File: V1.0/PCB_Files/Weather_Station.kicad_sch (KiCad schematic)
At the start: 13 parts, among them U1 STM32F103C8T6

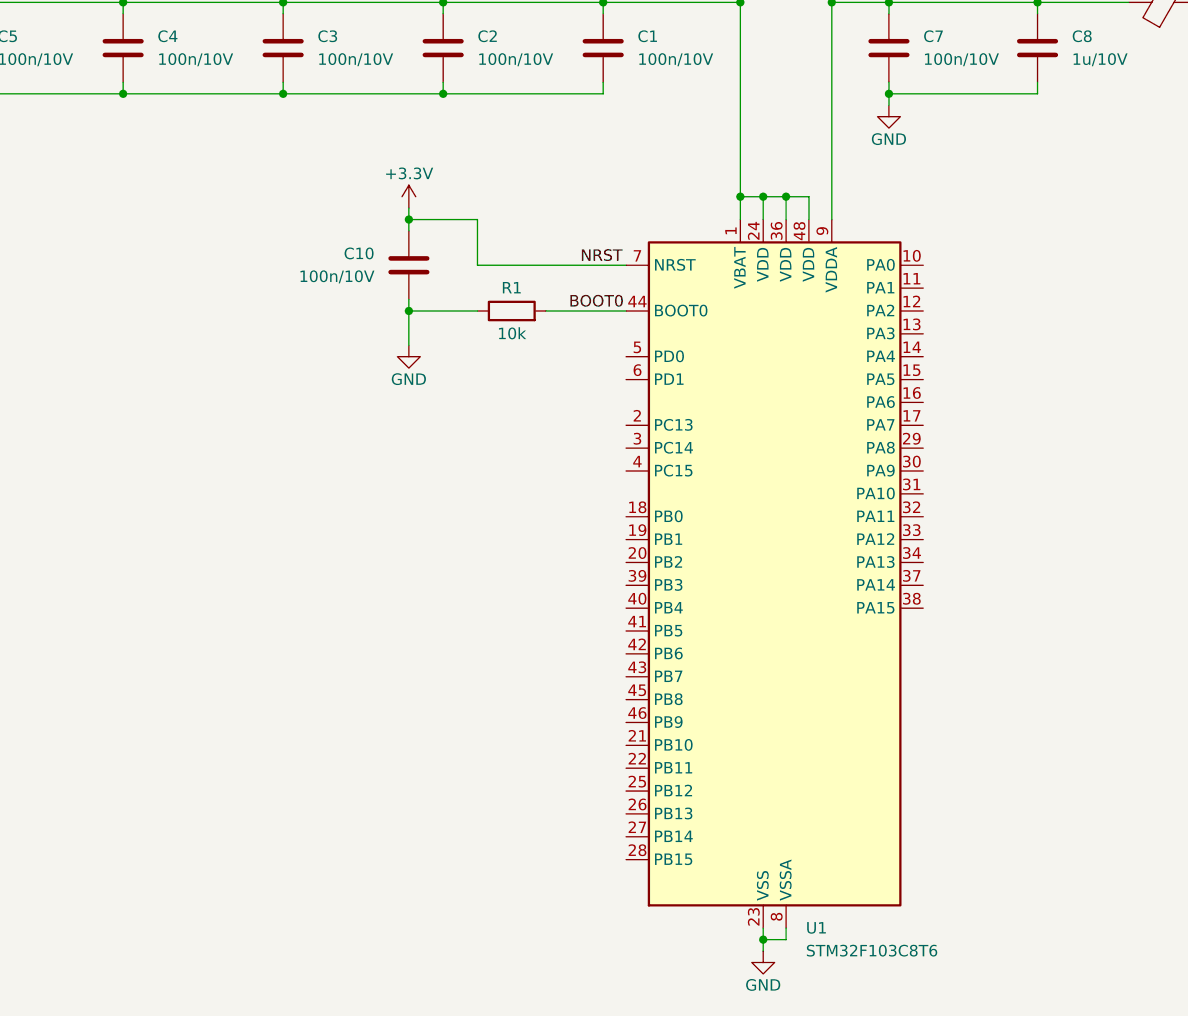
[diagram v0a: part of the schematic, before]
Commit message: Added STM32 Fiormware Directory + Prj. . Added OSC.
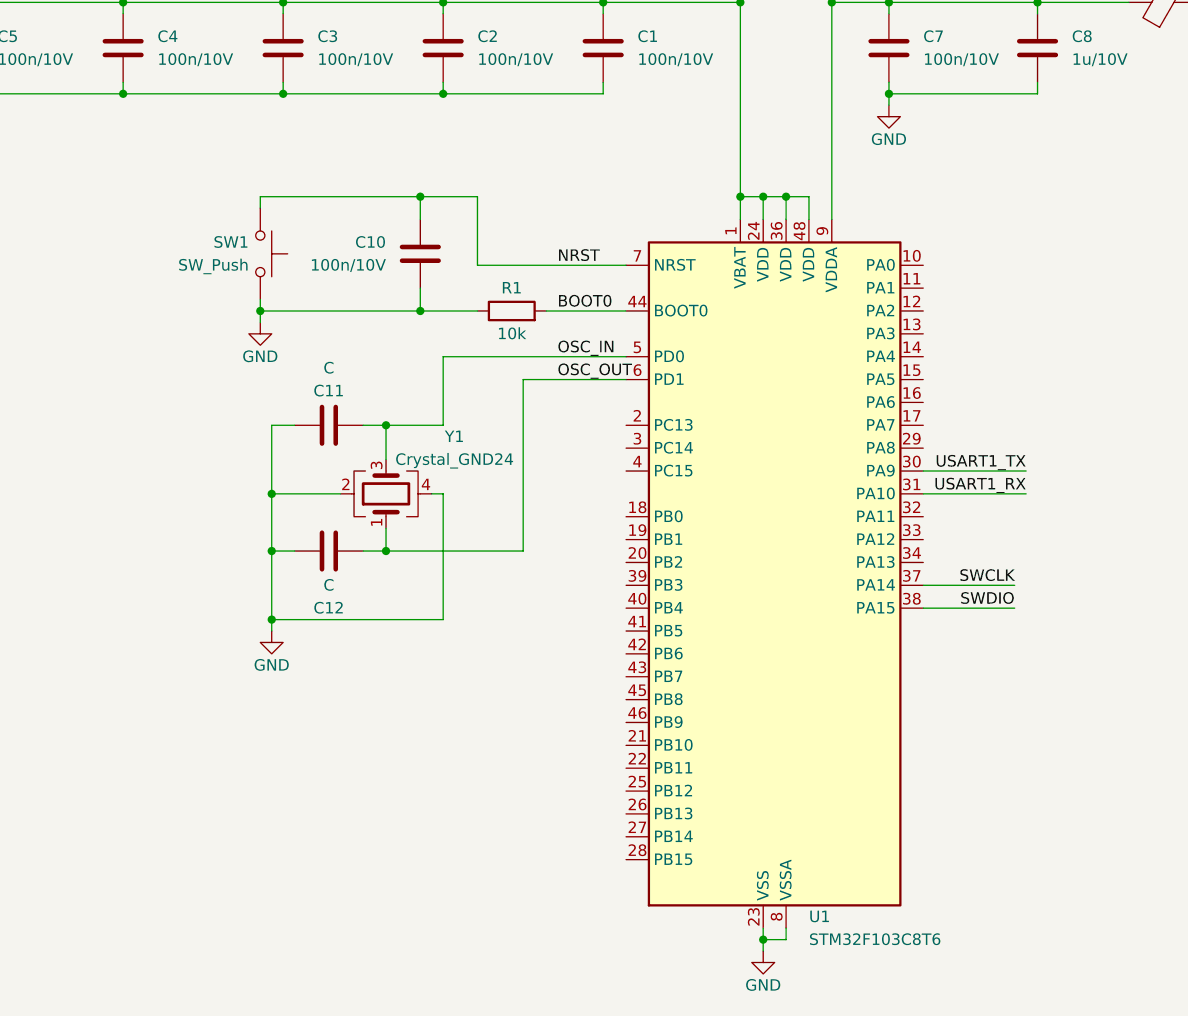
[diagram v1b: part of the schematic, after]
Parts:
- added C11, C12: C, symbol Device:C
- added SW1: SW_Push, symbol Switch:SW_Push
- added Y1: Crystal_GND24, symbol Device:Crystal_GND24
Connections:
- net +3.3V: no longer C10.2, U1.7 (NRST)
- net GND: now also C11.1, C12.2, SW1.2, Y1.2, Y1.4
- net USART1_TX: now reaches U1.30 (PA9)
- net USART1_RX: now reaches U1.31 (PA10)
- net SWCLK: now reaches U1.37 (PA14)
- net SWDIO: now reaches U1.38 (PA15)
- net OSC_IN: now reaches U1.5 (PD0)
- net OSC_IN: now also C11.2, Y1.3
- net OSC_OUT: now reaches U1.6 (PD1)
- net OSC_OUT: now also C12.1, Y1.1
- new net NRST: C10.2, SW1.1, U1.7 (NRST)
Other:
- moved on the sheet: C10

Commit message: Some changes in the IOC and continues Schematic.
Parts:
- added R2, R3: R, symbol Device:R
- added U2: HDC1080DMBR, Package_SON:Texas_PWSON-N6, symbol Sensor_Humidity:HDC1080
- added U3: NHD-C12832A1Z-FSRGB, Display:HY1602E, symbol Display_Graphic:NHD-C12832A1Z-FSRGB
- C11, C12: value C -> 10p/10V
- Y1: value Crystal_GND24 -> X322516MLB4SI
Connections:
- net +3.3V: now also R2.1, R3.1, U2.5 (VCC)
- net GND: now also C12.1, U2.2 (GND); no longer C12.2
- net OSC_OUT: now also C12.2; no longer C12.1
- net I2C1_SCL: now reaches U1.42 (PB6)
- net I2C1_SCL: now also R3.2, U2.6 (SCL)
- net I2C1_SDA: now reaches U1.43 (PB7)
- net I2C1_SDA: now also R2.2, U2.1 (SDA)
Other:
- note added: "Display"
- note added: "Display Stecker auch extern einfügen, falls display nicht geht, dass getestet werden kann."
- note added: "STM32"
- note added: "Sensor"
- note added: "ToDo: Calculate Resistor Values."
- moved on the sheet: C1, C10, C11, C2, C3, C4, C5, C6, C7, C8, C9, FB1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

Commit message: Display Wiring should be finsihed.
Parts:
- removed U3: NHD-C12832A1Z-FSRGB, Display:HY1602E, symbol Display_Graphic:NHD-C12832A1Z-FSRGB
- added C13, C14: 4u7/16V, symbol Device:C
- added C15: 2u2/16V, symbol Device:C
- added C16, C17: 1u/16V, symbol Device:C
- added C18: 100n/10V, symbol Device:C
- added C19, C20: 4u7/10V, symbol Device:C
- added J1: N091-2832TSWFG02-H14, symbol Connector:Conn_01x14_Socket
- added R4: 910k, symbol Device:R
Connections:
- net +3.3V: now also C13.1, C14.1, C18.1, C19.1, C20.1, J1.14 (Pin_14), J1.5 (Pin_5), J1.8 (Pin_8), J1.9 (Pin_9)
- net GND: now also C13.2, C14.2, C15.2, C18.2, C19.2, C20.2, J1.7 (Pin_7), R4.2
- new net C1N: C17.2, J1.4 (Pin_4)
- new net C1P: C17.1, J1.3 (Pin_3)
- new net C2N: C16.2, J1.2 (Pin_2)
- new net C2P: C16.1, J1.1 (Pin_1)
- new net IREF: J1.12 (Pin_12), R4.1
- new net SCL: J1.10 (Pin_10)
- new net SDA: J1.11 (Pin_11)
- new net VCOMH: C15.1, J1.13 (Pin_13)
- no-connect marks 0 -> 1
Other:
- note added: "Display Stiftleisten auch extern einfügen, falls display nicht geht, dass getestet werden kann."
- note added: "R4 nochmal checken."
- note removed: "Display Stecker auch extern einfügen, falls display nicht geht, dass getestet werden kann."

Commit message: Now Display should be finished.
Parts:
- C14: value 4u7/16V -> 100n/16V

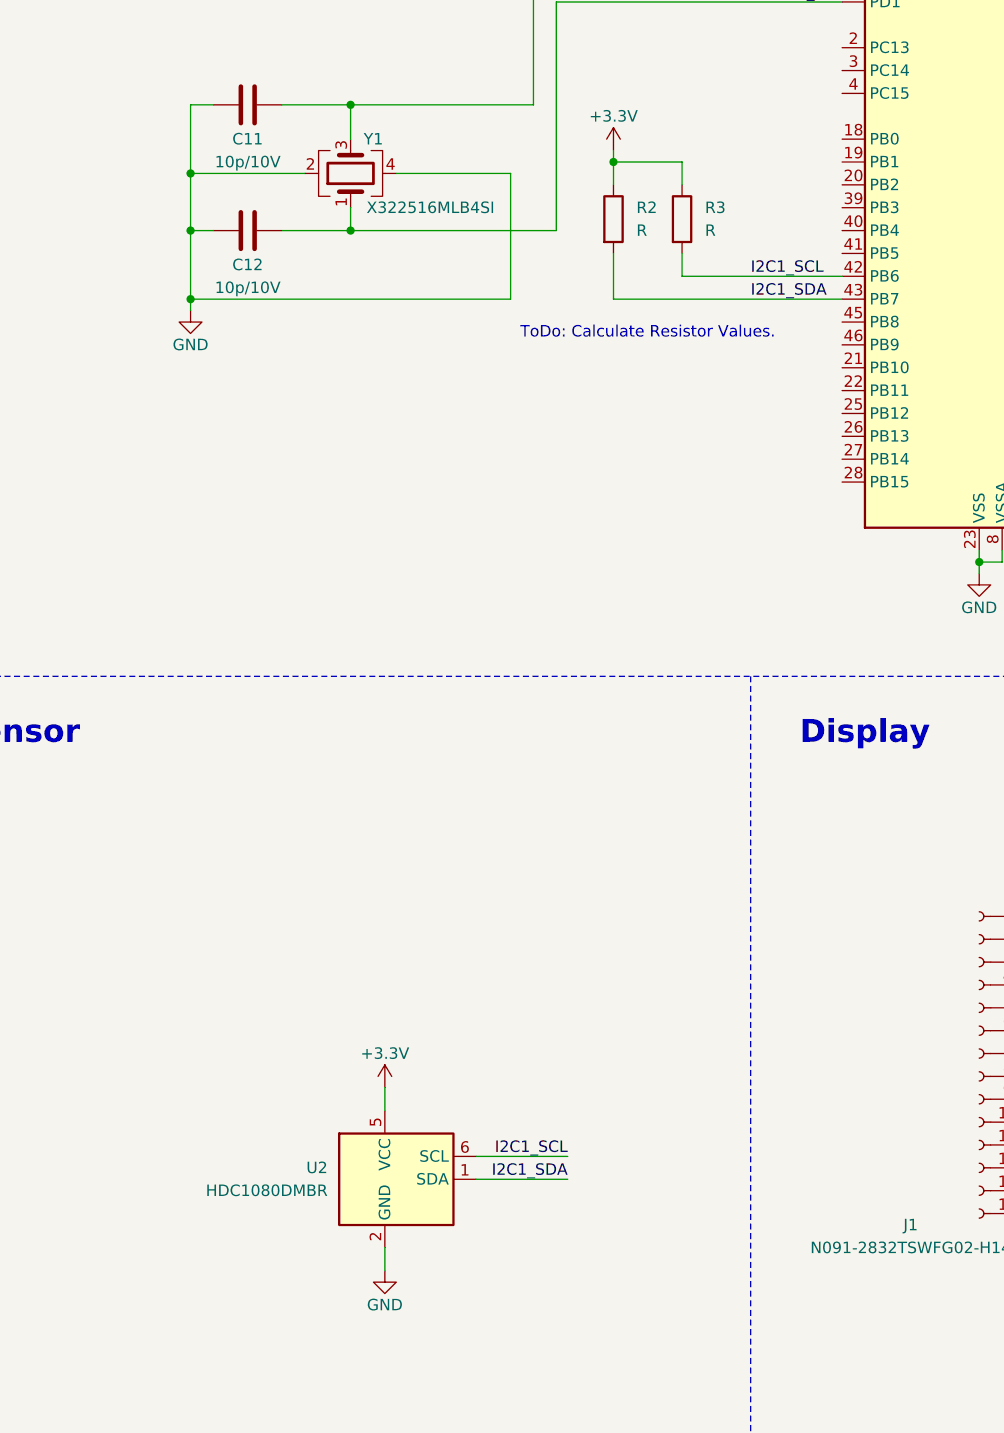
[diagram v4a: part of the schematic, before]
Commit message: Just added input capacitor to sensor.
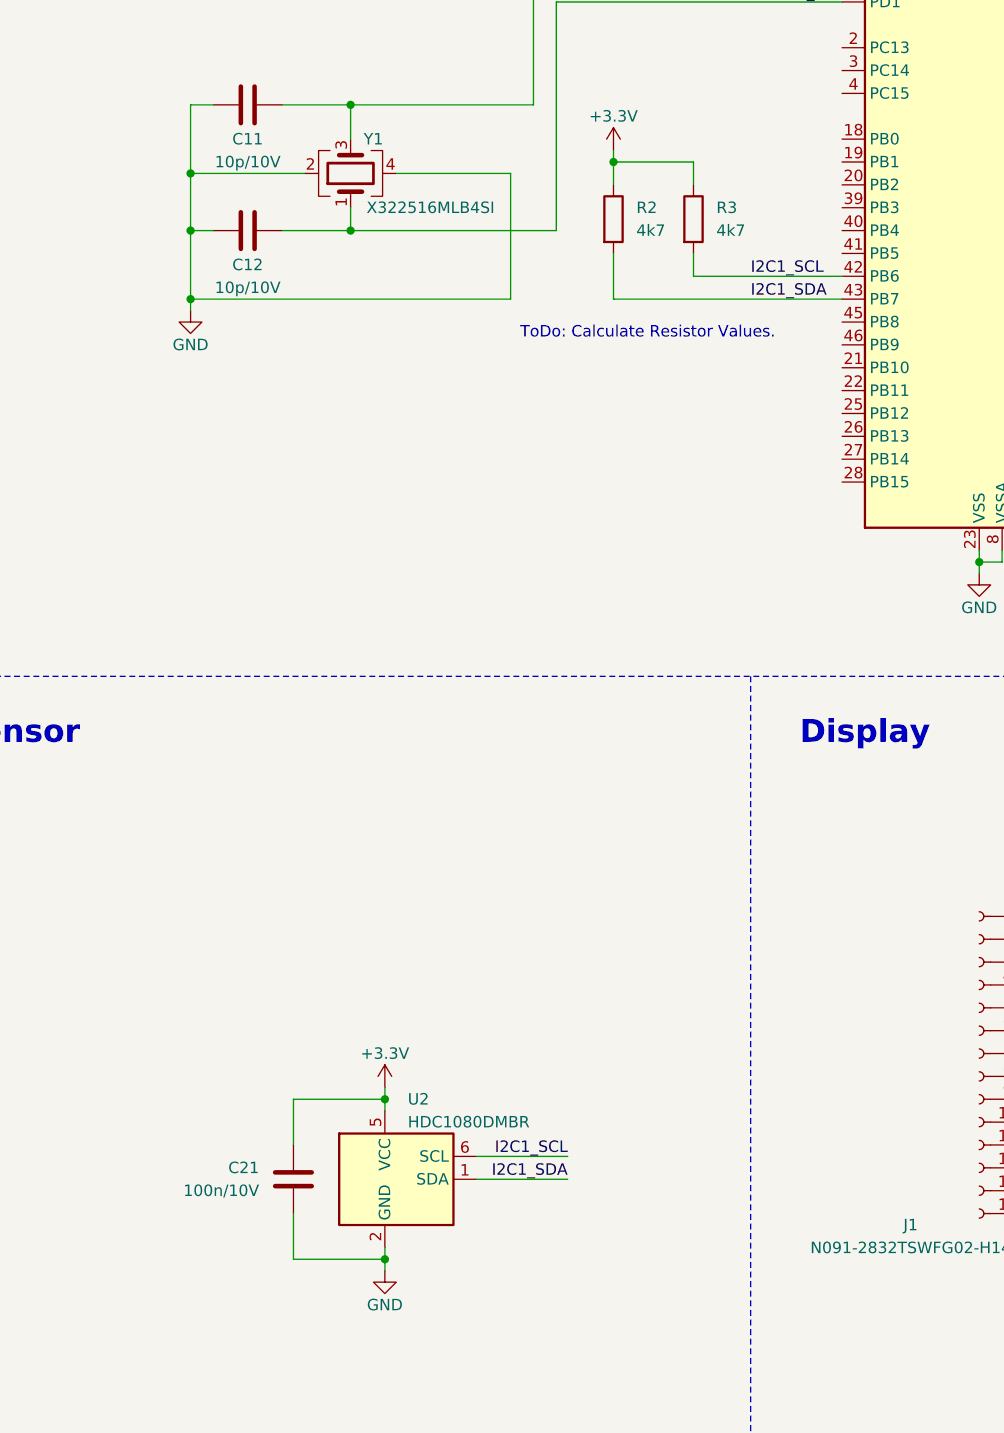
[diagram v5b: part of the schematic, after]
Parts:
- added C21: 100n/10V, symbol Device:C
- R2, R3: value R -> 4k7
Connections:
- net +3.3V: now also C21.2
- net GND: now also C21.1
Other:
- moved on the sheet: R3
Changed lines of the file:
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@@
 	)
 	(junction
+		(at 63.5 218.44)
+		(diameter 0)
+		(color 0 0 0 0)
+	)
+	(junction
 		(at 160.02 36.83)
 		(diameter 0)
@@
 	)
 	(junction
+		(at 63.5 200.66)
+		(diameter 0)
+		(color 0 0 0 0)
+	)
+	(junction
 		(at 193.04 223.52)
 		(diameter 0)
@@
 	(wire
 		(pts
-			(xy 96.52 106.68) (xy 96.52 109.22)
+			(xy 97.79 106.68) (xy 97.79 109.22)
 		)
 		(stroke
@@
 	(wire
 		(pts
-			(xy 88.9 96.52) (xy 96.52 96.52)
+			(xy 88.9 96.52) (xy 97.79 96.52)
 		)
 		(stroke
@@
 	(wire
 		(pts
-			(xy 96.52 109.22) (xy 114.3 109.22)
+			(xy 97.79 109.22) (xy 114.3 109.22)
 		)
 		(stroke
@@
 	(wire
 		(pts
-			(xy 63.5 199.39) (xy 63.5 201.93)
+			(xy 63.5 199.39) (xy 63.5 200.66)
 		)
 		(stroke
@@
 	(wire
 		(pts
-			(xy 96.52 96.52) (xy 96.52 99.06)
+			(xy 97.79 96.52) (xy 97.79 99.06)
 		)
 		(stroke
@@
 	(wire
 		(pts
+			(xy 53.34 205.74) (xy 53.34 200.66)
+		)
+		(stroke
+			(width 0)
+			(type default)
+		)
+	)
+	(wire
+		(pts
 			(xy 41.91 97.79) (xy 54.61 97.79)
 		)
@@
 	(wire
 		(pts
+			(xy 53.34 218.44) (xy 63.5 218.44)
+		)
+		(stroke
+			(width 0)
+			(type default)
+		)
+	)
+	(wire
+		(pts
 			(xy 129.54 140.97) (xy 132.08 140.97)
 		)
@@
 	(wire
 		(pts
+			(xy 53.34 200.66) (xy 63.5 200.66)
+		)
+		(stroke
+			(width 0)
+			(type default)
+		)
+	)
+	(wire
+		(pts
 			(xy 186.69 36.83) (xy 186.69 38.1)
 		)
@@
 	(wire
 		(pts
-			(xy 63.5 217.17) (xy 63.5 219.71)
+			(xy 63.5 218.44) (xy 63.5 219.71)
+		)
+		(stroke
+			(width 0)
+			(type default)
+		)
+	)
+	(wire
+		(pts
+			(xy 63.5 217.17) (xy 63.5 218.44)
 		)
 		(stroke
@@
 	(wire
 		(pts
+			(xy 53.34 213.36) (xy 53.34 218.44)
+		)
+		(stroke
+			(width 0)
+			(type default)
+		)
+	)
+	(wire
+		(pts
 			(xy 59.69 90.17) (xy 59.69 93.98)
 		)
@@
 	(wire
 		(pts
+			(xy 63.5 200.66) (xy 63.5 201.93)
+		)
+		(stroke
+			(width 0)
+			(type default)
+		)
+	)
+	(wire
+		(pts
 			(xy 137.16 200.66) (xy 137.16 198.12)
 		)
@@
 			)
 		)
-		(property "Value" "R"
+		(property "Value" "4k7"
 			(at 91.44 104.1399 0)
 			(effects
@@
 	)
 	(symbol
+		(lib_id "Device:C")
+		(at 53.34 209.55 0)
+		(mirror x)
+		(unit 1)
+		(exclude_from_sim no)
+		(in_bom yes)
+		(on_board yes)
+		(dnp no)
+		(property "Reference" "C21"
+			(at 49.53 208.2799 0)
+			(effects
+				(font
+					(size 1.27 1.27)
+				)
+				(justify right)
+			)
+		)
+		(property "Value" "100n/10V"
+			(at 49.53 210.8199 0)
+			(effects
+				(font
+					(size 1.27 1.27)
+				)
+				(justify right)
+			)
+		)
+		(property "Footprint" ""
+			(at 54.3052 205.74 0)
+			(effects
+				(font
+					(size 1.27 1.27)
+				)
+				(hide yes)
+			)
+		)
+		(property "Datasheet" "~"
+			(at 53.34 209.55 0)
+			(effects
+				(font
+					(size 1.27 1.27)
+				)
+				(hide yes)
+			)
+		)
+		(property "Description" "Unpolarized capacitor"
+			(at 53.34 209.55 0)
+			(effects
+				(font
+					(size 1.27 1.27)
+				)
+				(hide yes)
+			)
+		)
+		(pin "2"
+		)
+		(pin "1"
+		)
+		(instances
+			(project "Weather_Station"
+				(path "/480d2398-431a-4c09-b50a-21d5fdc9f45a"
+					(reference "C21")
+					(unit 1)
+				)
+			)
+		)
+	)
+	(symbol
 		(lib_id "Connector:Conn_01x14_Socket")
 		(at 129.54 195.58 0)
@@
 		(on_board yes)
 		(dnp no)
-		(fields_autoplaced yes)
 		(property "Reference" "U2"
-			(at 57.15 208.2799 0)
+			(at 66.04 200.66 0)
 			(effects
 				(font
 					(size 1.27 1.27)
 				)
-				(justify right)
+				(justify left)
 			)
 		)
 		(property "Value" "HDC1080DMBR"
-			(at 57.15 210.8199 0)
+			(at 66.04 203.2 0)
 			(effects
 				(font
 					(size 1.27 1.27)
 				)
-				(justify right)
+				(justify left)
 			)
 		)
@@
 	(symbol
 		(lib_id "Device:R")
-		(at 96.52 102.87 0)
+		(at 97.79 102.87 0)
 		(unit 1)
 		(exclude_from_sim no)
@@
 		(fields_autoplaced yes)
 		(property "Reference" "R3"
-			(at 99.06 101.5999 0)
+			(at 100.33 101.5999 0)
 			(effects
 				(font
@@
 			)
 		)
-		(property "Value" "R"
-			(at 99.06 104.1399 0)
+		(property "Value" "4k7"
+			(at 100.33 104.1399 0)
 			(effects
 				(font
@@
 		)
 		(property "Footprint" ""
-			(at 94.742 102.87 90)
+			(at 96.012 102.87 90)
 			(effects
 				(font
@@
 		)
 		(property "Datasheet" "~"
-			(at 96.52 102.87 0)
+			(at 97.79 102.87 0)
 			(effects
 				(font
@@
 		)
 		(property "Description" "Resistor"
-			(at 96.52 102.87 0)
+			(at 97.79 102.87 0)
 			(effects
 				(font

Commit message: Added Step File of Sensor. USB Section should be finished and be ready for design.
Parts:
- removed J1: N091-2832TSWFG02-H14, symbol Connector:Conn_01x14_Socket
- removed SW1: SW_Push, symbol Switch:SW_Push
- added C22: 10uF/10V, symbol Device:C
- added C23: C, symbol Device:C
- added D1: ESDA7P60-1U1M, Diode_SMD:ST_QFN-2L_1.6x1.0mm, symbol Device:D_TVS
- added F1: JFC1206-1100FS, Fuse:Fuse_1206_3216Metric, symbol Device:Fuse
- added J1: N091-2832TSWFG02-H14, Private_Connector_Display:OLED_SMD_128x32, symbol Connector:Conn_01x14_Pin
- added J2: USB_B_Micro, Connector_USB:USB_Mini-B_Lumberg_2486_01_Horizontal, symbol Connector:USB_B_Micro
- added J3: Conn_01x04_Pin, Connector_PinHeader_1.00mm:PinHeader_1x04_P1.00mm_Vertical, symbol Connector:Conn_01x04_Pin
- added R5: 1k5, Resistor_SMD:R_0603_1608Metric, symbol Device:R
- added U3: AMS1117-3.3, Package_TO_SOT_SMD:SOT-223-3_TabPin2, symbol Regulator_Linear:AMS1117-3.3
- added U5: SRV05-4, Package_TO_SOT_SMD:SOT-23-6, symbol Power_Protection:SRV05-4
- C1, C10, C11, C12, C14, C16, C17, C18, C2, C21, C3, C4, C5, C7, C8, C9: footprint (none) -> Capacitor_SMD:C_0603_1608Metric
- C13, C15, C19, C20, C6: footprint (none) -> Capacitor_SMD:C_0805_2012Metric
- FB1: footprint (none) -> Inductor_SMD:L_1206_3216Metric
- R1, R2, R3, R4: footprint (none) -> Resistor_SMD:R_0603_1608Metric
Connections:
- net +3.3V: now also C23.1, J1.14 (Pin_14), J1.5 (Pin_5), J1.8 (Pin_8), J1.9 (Pin_9), J3.3 (Pin_3), U3.2 (VO)
- net C1N: now also J1.4 (Pin_4)
- net C1P: now also J1.3 (Pin_3)
- net C2N: now also J1.2 (Pin_2)
- net C2P: now also J1.1 (Pin_1)
- net GND: now also C22.2, C23.2, D1.1 (A1), J1.7 (Pin_7), J2.5 (GND), J3.4 (Pin_4), U3.1 (GND), U5.2 (VN)
- net I2C1_SCL: now also J1.10 (Pin_10), J3.2 (Pin_2)
- net I2C1_SDA: now also J1.11 (Pin_11), J3.1 (Pin_1)
- net IREF: now also J1.12 (Pin_12)
- net VCOMH: now also J1.13 (Pin_13)
- net USB_DM: now reaches U1.32 (PA11)
- net USB_DM: now also U5.1 (IO1)
- net USB_DP: now reaches U1.33 (PA12)
- net USB_DP: now also U5.3 (IO2)
- new net: D1.2 (A2), F1.2, J2.1 (VBUS), R5.1, U5.5 (VP)
- new net: J2.3 (D+), R5.2
- new net USB_DM_IN: J2.2 (D-), U5.4 (IO3)
- new net USB_DP_IN: J2.4 (ID), U5.6 (IO4)
- new net VBUS: C22.1, F1.1, U3.3 (VI)
- no-connect marks 1 -> 2
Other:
- note added: "Display - Backup"
- note added: "LDO 5V -> 3.3V"
- note added: "Noch nach einer Alternative für Diode suchen."
- note added: "USB-B_Micro"
- moved on the sheet: C10, R1
